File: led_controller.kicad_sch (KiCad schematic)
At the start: 8 parts, among them M1 3V/6V/12V

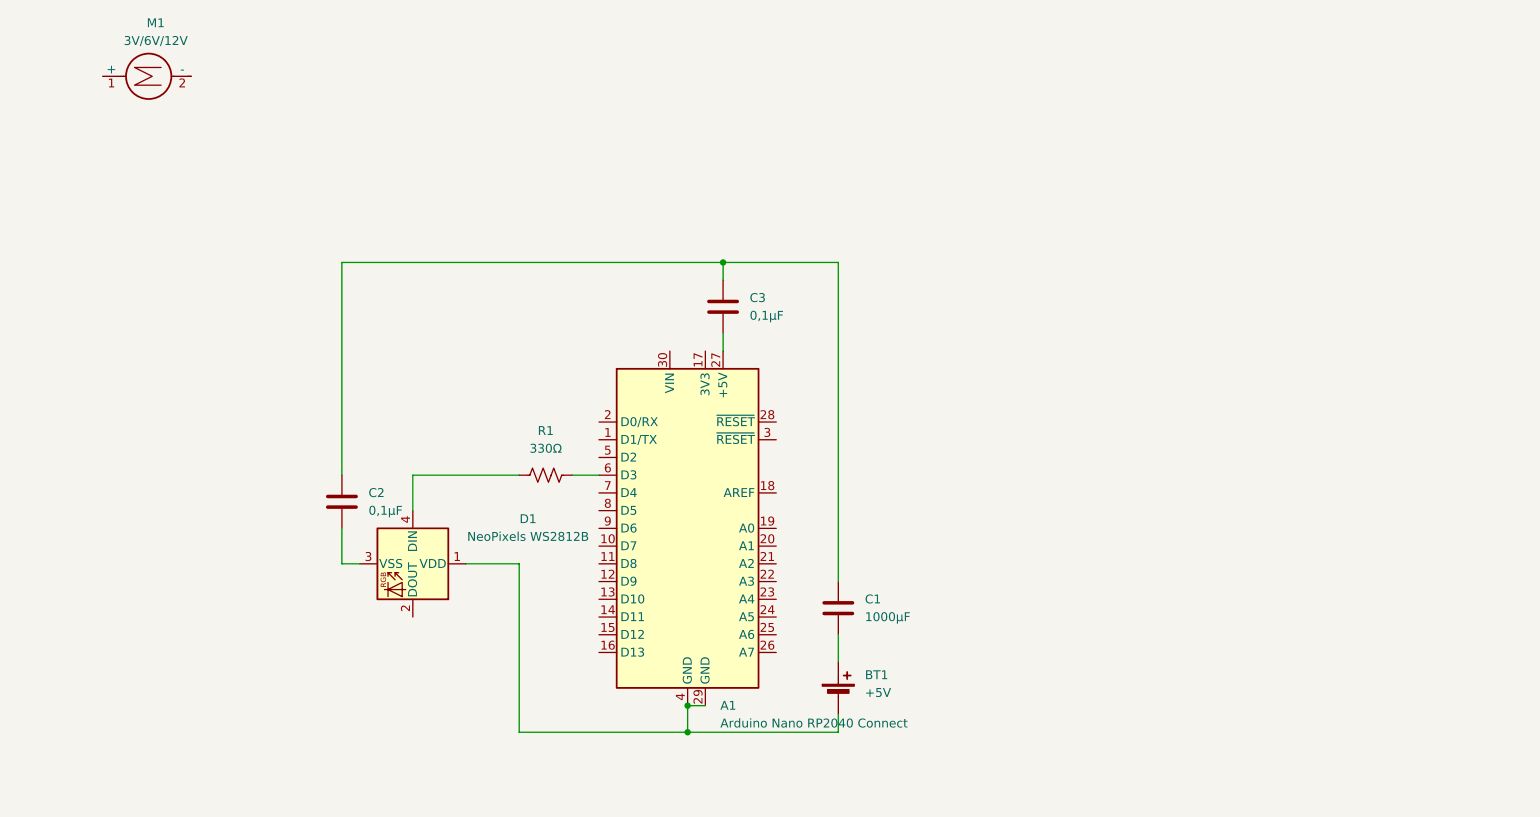
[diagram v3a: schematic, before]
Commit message: add all neopixels in parallel
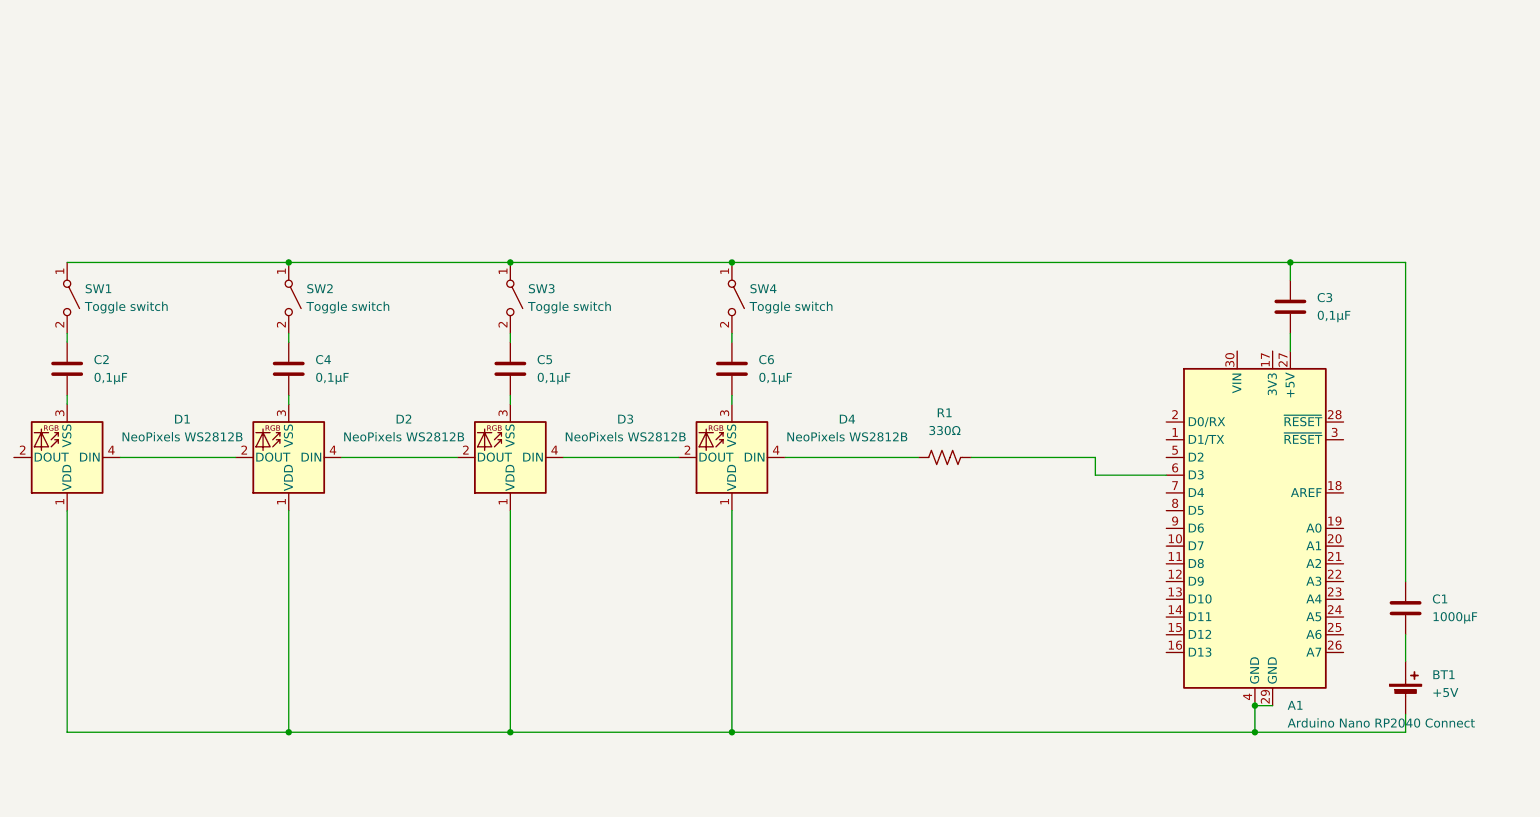
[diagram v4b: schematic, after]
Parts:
- removed M1: 3V/6V/12V, symbol Motor:Motor_DC
- added C4, C5, C6: 0,1µF, symbol Device:C
- added D2, D3, D4: NeoPixels WS2812B, LED_SMD:LED_WS2812B_PLCC4_5.0x5.0mm_P3.2mm, symbol LED:WS2812B
- added SW1, SW2, SW3, SW4: Toggle switch, symbol Switch:SW_SPST
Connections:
- net at C1.2, C3.1: now also SW1.1 (A), SW2.1 (A), SW3.1 (A), SW4.1 (A); no longer C2.1
- net at A1.29 (GND), A1.4 (GND), BT1.2 (-)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: now also D2.1 (VDD), D3.1 (VDD), D4.1 (VDD)
- net at D1.4 (DIN): now also D2.2 (DOUT); no longer R1.1
- new net: C6.1, SW4.2 (B)
- new net: C6.2, D4.3 (VSS)
- new net: C4.2, D2.3 (VSS)
- new net: D2.4 (DIN), D3.2 (DOUT)
- new net: D4.4 (DIN), R1.1
- new net: D3.4 (DIN), D4.2 (DOUT)
- new net: C2.1, SW1.2 (B)
- new net: C5.1, SW3.2 (B)
- new net: C5.2, D3.3 (VSS)
- new net: C4.1, SW2.2 (B)
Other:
- moved on the sheet: A1, BT1, C1, C3
